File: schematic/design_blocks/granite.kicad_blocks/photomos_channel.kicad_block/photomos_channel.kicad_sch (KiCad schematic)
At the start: 3 parts, among them K1 TLP176A

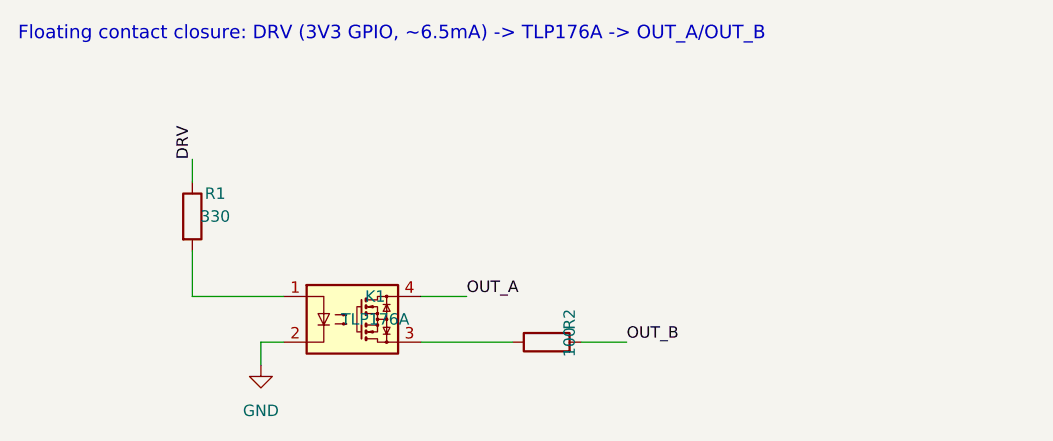
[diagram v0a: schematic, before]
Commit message: Fix photoMOS package and part, ethernet crystal
Signed-off-by: Lee Smet <lee.smet@hotmail.com>
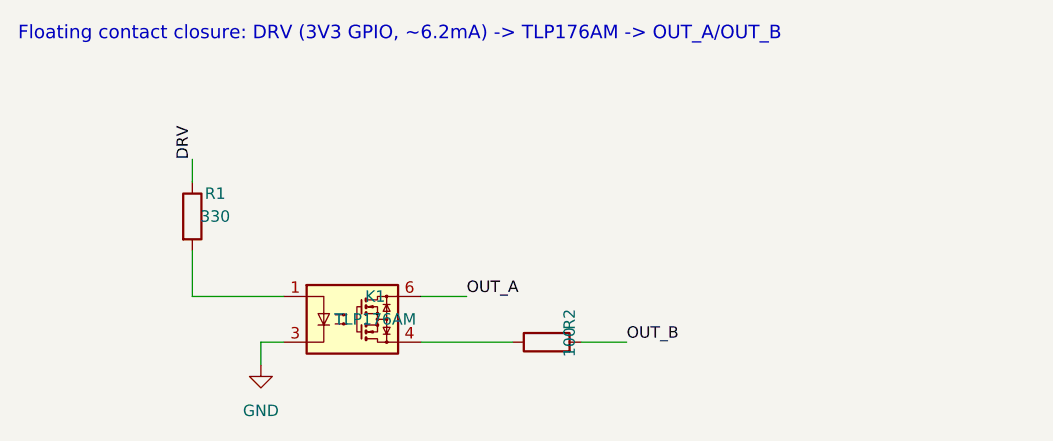
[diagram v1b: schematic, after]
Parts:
- K1: value TLP176A -> TLP176AM; footprint Package_SO:SOP-4_3.8x4.1mm_P2.54mm -> Package_SO:SOIC-4_4.55x3.7mm_P2.54mm; symbol Relay_SolidState:CPC1017N -> granite:TLP176AM
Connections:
- net GND: now also K1.3; no longer K1.2
- net OUT_A: now also K1.6; no longer K1.4
- net at R2.1: now also K1.4; no longer K1.3
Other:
- note added: "Floating contact closure: DRV (3V3 GPIO, ~6.2mA) -> TLP176AM -> OUT_A/OUT_B"
- note removed: "Floating contact closure: DRV (3V3 GPIO, ~6.5mA) -> TLP176A -> OUT_A/OUT_B"
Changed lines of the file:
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@@
 		(comment 1 "PoE-powered reset/power controller for 14 Strix Halo motherboards")
 	)
-	(text "Floating contact closure: DRV (3V3 GPIO, ~6.5mA) -> TLP176A -> OUT_A/OUT_B"
+	(text "Floating contact closure: DRV (3V3 GPIO, ~6.2mA) -> TLP176AM -> OUT_A/OUT_B"
 		(exclude_from_sim no)
 		(at 20 20 0)
@@
 	)
 	(symbol
-		(lib_id "Relay_SolidState:CPC1017N")
+		(lib_id "granite:TLP176AM")
 		(at 57.15 50.8 0)
 		(unit 1)
@@
 			)
 		)
-		(property "Value" "TLP176A"
+		(property "Value" "TLP176AM"
 			(at 59.69 50.8 0)
 			(effects
@@
 			)
 		)
-		(property "Footprint" "Package_SO:SOP-4_3.8x4.1mm_P2.54mm"
+		(property "Footprint" "Package_SO:SOIC-4_4.55x3.7mm_P2.54mm"
 			(at 57.15 50.8 0)
 			(effects
@@
 		(pin "1"
 		)
-		(pin "2"
-		)
 		(pin "3"
 		)
 		(pin "4"
 		)
+		(pin "6"
+		)
 		(instances
